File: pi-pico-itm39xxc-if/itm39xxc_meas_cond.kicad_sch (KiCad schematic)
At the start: 25 parts

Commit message: Working on pico itm interface
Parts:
- R? (x2): value 24k -> 20k
- R? (x2): value 12k -> 10k
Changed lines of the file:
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@@
       (effects (font (size 1.27 1.27)) (justify left))
     )
-    (property "Value" "24k" (id 1) (at 88.011 27.94 90)
+    (property "Value" "20k" (id 1) (at 88.011 27.94 90)
       (effects (font (size 1.27 1.27)) (justify left))
     )
@@
       (effects (font (size 1.27 1.27)) (justify left))
     )
-    (property "Value" "12k" (id 1) (at 36.703 82.296 0)
+    (property "Value" "10k" (id 1) (at 36.703 82.296 0)
       (effects (font (size 1.27 1.27)) (justify left))
     )
@@
       (effects (font (size 1.27 1.27)) (justify left))
     )
-    (property "Value" "12k" (id 1) (at 33.401 64.008 90)
+    (property "Value" "10k" (id 1) (at 33.401 64.008 90)
       (effects (font (size 1.27 1.27)) (justify left))
     )
@@
       (effects (font (size 1.27 1.27)) (justify left))
     )
-    (property "Value" "24k" (id 1) (at 91.313 46.228 0)
+    (property "Value" "20k" (id 1) (at 91.313 46.228 0)
       (effects (font (size 1.27 1.27)) (justify left))
     )

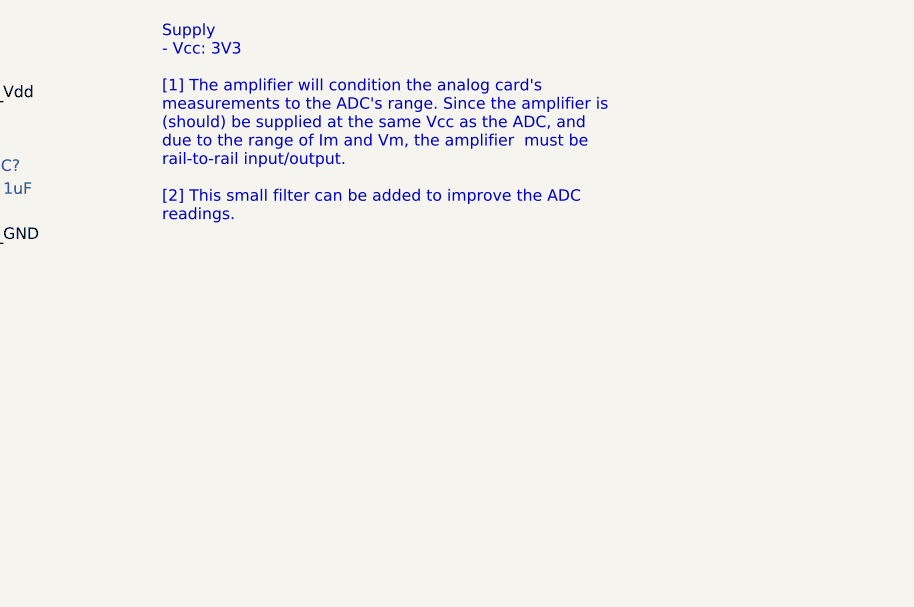
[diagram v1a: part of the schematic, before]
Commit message: Added docs for subcircuits
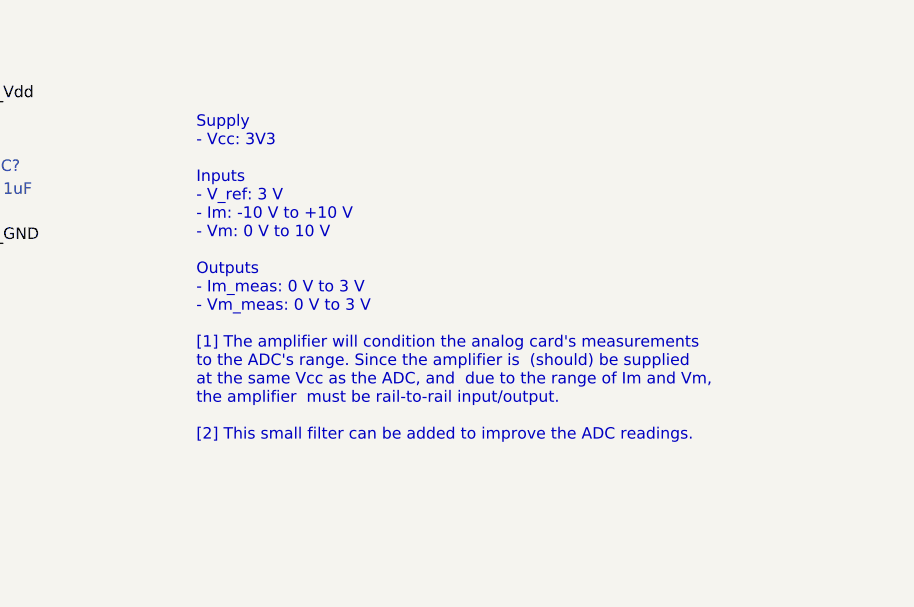
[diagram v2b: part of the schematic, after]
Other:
- note added: "Supply - Vcc: 3V3 Inputs - V_ref: 3 V - Im: -10 V to +10 V - Vm: 0 V to 10 V Outputs - Im_meas: 0 V to 3 V - Vm_meas: 0 V to 3 V [1] The amplifier will condition the analog card's measurements to the ADC's range. Since the amplifier is (should) be supplied at the same Vcc as the ADC, and due to the range of Im and Vm, the amplifier must be rail-to-rail input/output. [2] This small filter can be a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"
- note removed: "Supply - Vcc: 3V3 [1] The amplifier will condition the analog card's measurements to the ADC's range. Since the amplifier is (should) be supplied at the same Vcc as the ADC, and due to the range of Im and Vm, the amplifier must be rail-to-rail input/output. [2] This small filter can be added to improve the ADC readings."
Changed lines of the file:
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@@
     (effects (font (size 1.27 1.27)) (justify left bottom))
   )
-  (text "Supply\n- Vcc: 3V3\n\n[1] The amplifier will condition the analog card's\nmeasurements to the ADC's range. Since the amplifier is \n(should) be supplied at the same Vcc as the ADC, and \ndue to the range of Im and Vm, the amplifier  must be \nrail-to-rail input/output.\n\n[2] This small filter can be added to improve the ADC\nreadings."
-    (at 168.402 40.132 0)
+  (text "Supply\n- Vcc: 3V3\n\nInputs\n- V_ref: 3 V\n- Im: -10 V to +10 V\n- Vm: 0 V to 10 V\n\nOutputs\n- Im_meas: 0 V to 3 V\n- Vm_meas: 0 V to 3 V\n\n[1] The amplifier will condition the analog card's measurements \nto the ADC's range. Since the amplifier is  (should) be supplied \nat the same Vcc as the ADC, and  due to the range of Im and Vm,\nthe amplifier  must be rail-to-rail input/output.\n\n[2] This small filter can be added to improve the ADC readings."
+    (at 172.212 64.516 0)
     (effects (font (size 1.27 1.27)) (justify left bottom))
   )

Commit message: Passing ERC
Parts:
- C32, C33, C34, C35, C36, C37, C38: renamed from C?; footprint Capacitor_SMD:C_0805_2012Metric -> Capacitor_SMD:C_0805_2012Metric_Pad1.18x1.45mm_HandSolder
- R36, R37, R38, R39, R40, R41, R42, R43, R44, R45, R46, R47: renamed from R?; footprint Resistor_SMD:R_0805_2012Metric -> Resistor_SMD:R_0805_2012Metric_Pad1.20x1.40mm_HandSolder
- U11: renamed from U?; footprint (none) -> Package_SO:SOIC-8_3.9x4.9mm_P1.27mm
- gave numbers to parts that had none: 2

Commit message: Working on pcb for pi pico it
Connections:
- net V_ref': now also U11.3 (+); no longer U11.5 (+)
- net at R43.2, R44.2: now also U11.5 (+); no longer U11.3 (+)
- net at R46.1, R47.1: now also U11.6 (-); no longer U11.2 (-)
- net at R45.1, R46.2: now also U11.7; no longer U11.1
- new net: U11.1, U11.2 (-)
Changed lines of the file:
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@@
     (pin "2")
   )
-  (symbol (lib_id "Device:Opamp_Dual") (at 44.577 68.326 0) (unit 1)
+  (symbol (lib_id "Device:Opamp_Dual") (at 44.577 68.326 0) (unit 2)
     (in_bom yes) (on_board yes)
     (property "Reference" "U11" (id 0) (at 47.625 65.278 0))
@@
     (pin "2")
   )
-  (symbol (lib_id "Device:Opamp_Dual") (at 91.44 69.596 0) (unit 2)
+  (symbol (lib_id "Device:Opamp_Dual") (at 91.44 69.596 0) (unit 1)
     (in_bom yes) (on_board yes)
     (property "Reference" "U11" (id 0) (at 91.44 64.516 0))
